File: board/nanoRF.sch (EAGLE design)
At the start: 21 parts

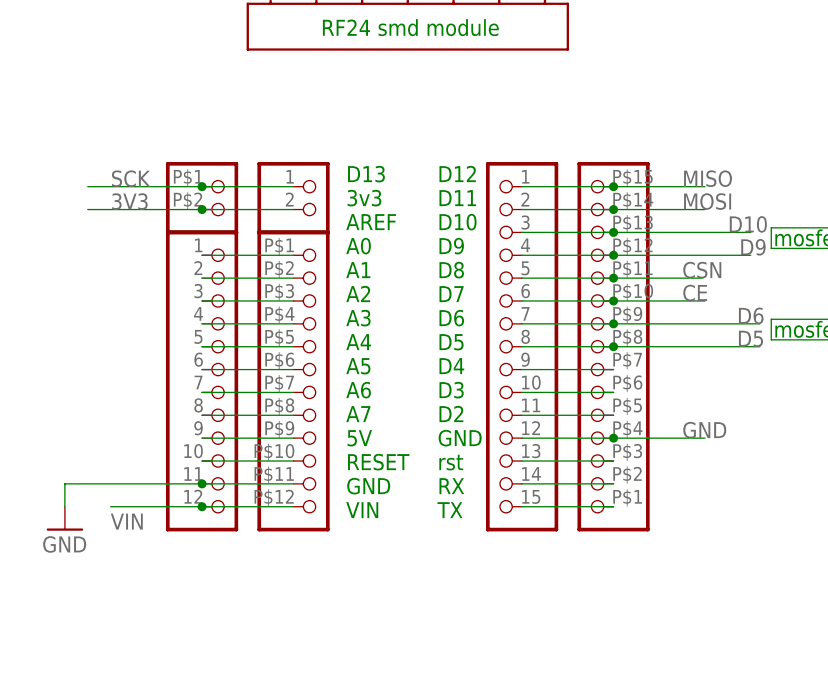
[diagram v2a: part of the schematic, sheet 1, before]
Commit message: removed reset and aref
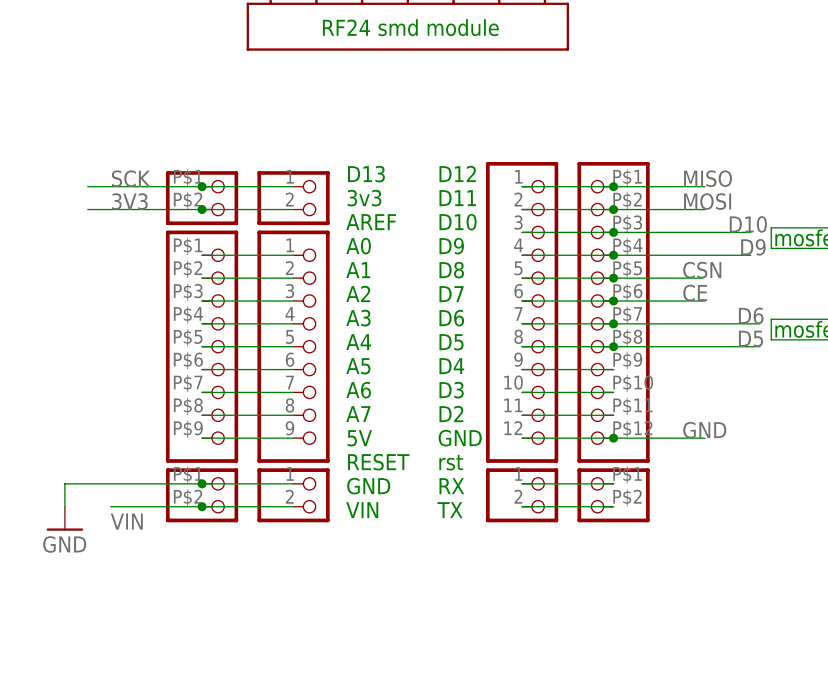
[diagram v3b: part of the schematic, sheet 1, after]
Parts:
- removed JP2: (no value), nano24rf:HEADER-1X15RND
- removed JP3: (no value), nano24rf:HEADER-1X15LONG
- added U$12, U$16: HEADER_1X2ROUND, nanoRF:HEADER_1X2ROUND
- added U$13, U$15: HEADER_1X2LONG, nanoRF:HEADER_1X2LONG
- added U$14: HEADER-1X12LONG, nanoRF:HEADER-1X12LONG
- added U$18: HEADER-1X12ROUND, nanoRF:HEADER-1X12ROUND
- U$6: value HEADER-1X12LONG -> HEADER-1X09RND; device nanoRF:HEADER-1X12LONG -> nanoRF:HEADER-1X09RND
- U$7: value HEADER-1X12ROUND -> HEADER-1X09LONG; device nanoRF:HEADER-1X12ROUND -> nanoRF:HEADER-1X09LONG
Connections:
- removed net N$10: U$6.10, U$7.10
- removed net N$13: JP2.13, JP3.3
- net CE: now also U$14.6, U$18.6; no longer JP2.6, JP3.10
- net CSN: now also U$14.5, U$18.5; no longer JP2.5, JP3.11
- net D10: now also U$14.3, U$18.3; no longer JP2.3, JP3.13
- net D5: now also U$14.8, U$18.8; no longer JP2.8, JP3.8
- net D6: now also U$14.7, U$18.7; no longer JP2.7, JP3.9
- net D9: now also U$14.4, U$18.4; no longer JP2.4, JP3.12
- net GND: now also U$12.1, U$13.1, U$14.12, U$18.12; no longer JP2.12, JP3.4, U$6.11, U$7.11
- net MISO: now also U$14.1, U$18.1; no longer JP2.1, JP3.15
- net MOSI: now also U$14.2, U$18.2; no longer JP2.2, JP3.14
- net N$11: now also U$15.2, U$16.2; no longer JP2.15, JP3.1
- net N$12: now also U$15.1, U$16.1; no longer JP2.14, JP3.2
- net N$14: now also U$14.11, U$18.11; no longer JP2.11, JP3.5
- net N$15: now also U$14.10, U$18.10; no longer JP2.10, JP3.6
- net N$16: now also U$14.9, U$18.9; no longer JP2.9, JP3.7
- net VIN: now also U$12.2, U$13.2; no longer U$6.12, U$7.12

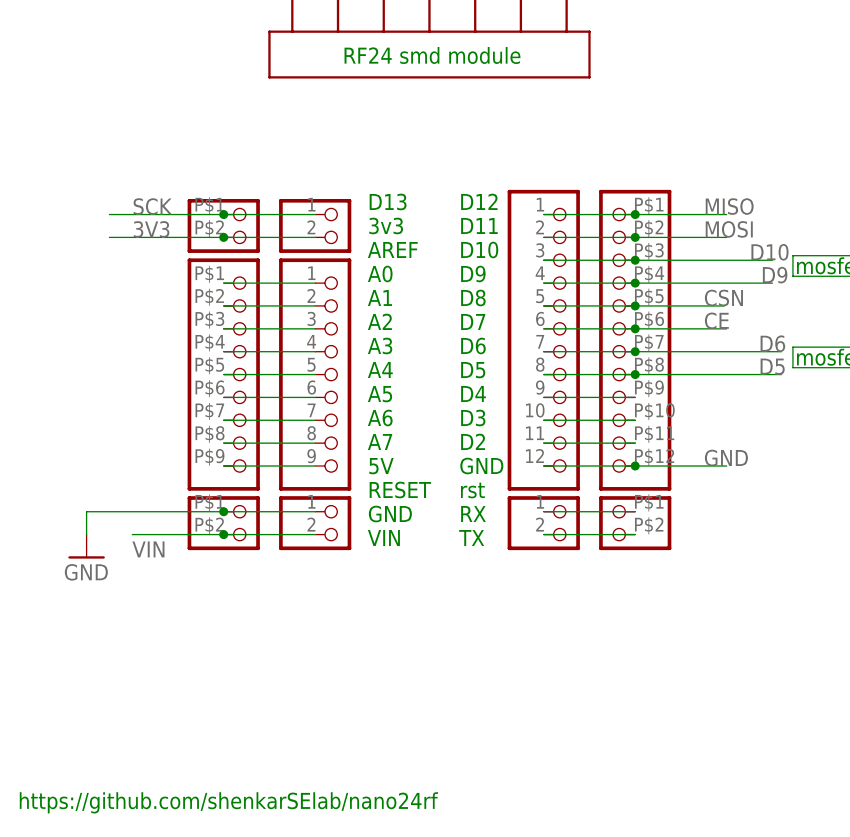
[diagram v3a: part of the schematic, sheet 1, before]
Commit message: revert to green ver, with gnd fix
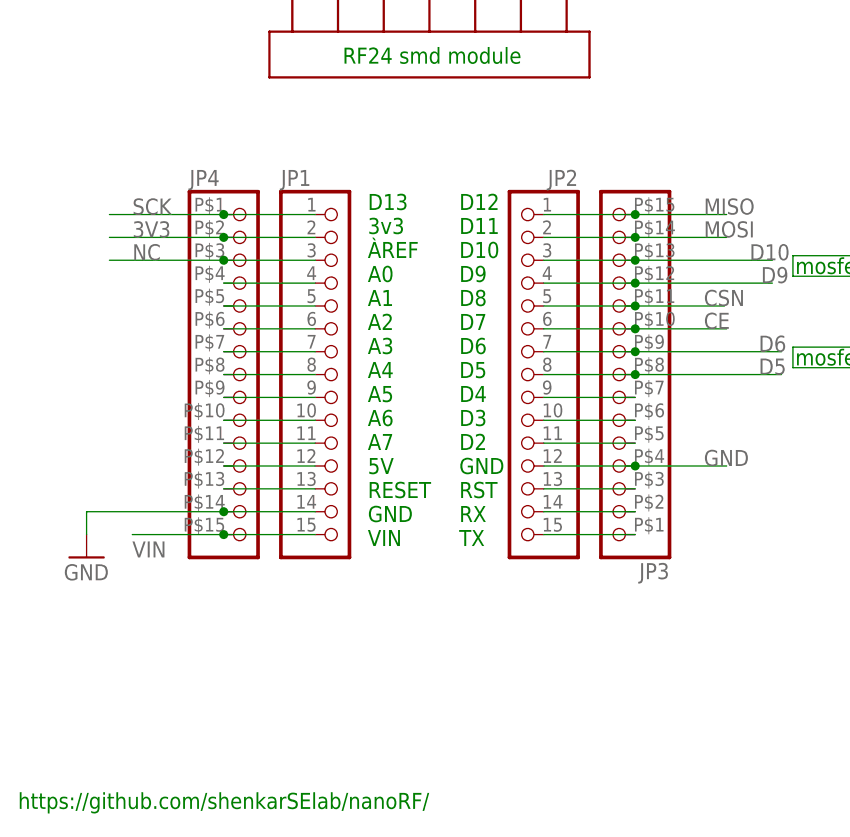
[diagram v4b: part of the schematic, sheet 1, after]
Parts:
- removed U$11, U$12, U$16: HEADER_1X2ROUND, nanoRF:HEADER_1X2ROUND
- removed U$13, U$15, U$8: HEADER_1X2LONG, nanoRF:HEADER_1X2LONG
- removed U$14: HEADER-1X12LONG, nanoRF:HEADER-1X12LONG
- removed U$18: HEADER-1X12ROUND, nanoRF:HEADER-1X12ROUND
- removed U$6: HEADER-1X09RND, nanoRF:HEADER-1X09RND
- removed U$7: HEADER-1X09LONG, nanoRF:HEADER-1X09LONG
- added JP1, JP2: (no value), nano24rf:HEADER-1X15RND
- added JP3, JP4: (no value), nano24rf:HEADER-1X15LONG
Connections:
- new net N$10: JP1.13, JP4.13
- new net N$13: JP2.13, JP3.3
- new net NC: JP1.3, JP4.3
- net 3V3: now also JP1.2, JP4.2; no longer U$11.2, U$8.2
- net CE: now also JP2.6, JP3.10; no longer U$14.6, U$18.6
- net CSN: now also JP2.5, JP3.11; no longer U$14.5, U$18.5
- net D10: now also JP2.3, JP3.13; no longer U$14.3, U$18.3
- net D5: now also JP2.8, JP3.8; no longer U$14.8, U$18.8
- net D6: now also JP2.7, JP3.9; no longer U$14.7, U$18.7
- net D9: now also JP2.4, JP3.12; no longer U$14.4, U$18.4
- net GND: now also JP1.14, JP2.12, JP3.4, JP4.14; no longer U$12.1, U$13.1, U$14.12, U$18.12
- net MISO: now also JP2.1, JP3.15; no longer U$14.1, U$18.1
- net MOSI: now also JP2.2, JP3.14; no longer U$14.2, U$18.2
- net N$1: now also JP1.4, JP4.4; no longer U$6.1, U$7.1
- net N$11: now also JP2.15, JP3.1; no longer U$15.2, U$16.2
- net N$12: now also JP2.14, JP3.2; no longer U$15.1, U$16.1
- net N$14: now also JP2.11, JP3.5; no longer U$14.11, U$18.11
- net N$15: now also JP2.10, JP3.6; no longer U$14.10, U$18.10
- net N$16: now also JP2.9, JP3.7; no longer U$14.9, U$18.9
- net N$2: now also JP1.5, JP4.5; no longer U$6.2, U$7.2
- net N$3: now also JP1.6, JP4.6; no longer U$6.3, U$7.3
- net N$4: now also JP1.7, JP4.7; no longer U$6.4, U$7.4
- net N$5: now also JP1.8, JP4.8; no longer U$6.5, U$7.5
- net N$6: now also JP1.9, JP4.9; no longer U$6.6, U$7.6
- net N$7: now also JP1.10, JP4.10; no longer U$6.7, U$7.7
- net N$8: now also JP1.11, JP4.11; no longer U$6.8, U$7.8
- net N$9: now also JP1.12, JP4.12; no longer U$6.9, U$7.9
- net SCK: now also JP1.1, JP4.1; no longer U$11.1, U$8.1
- net VIN: now also JP1.15, JP4.15; no longer U$12.2, U$13.2
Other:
- note added: "D12 D11 D10 D9 D8 D7 D6 D5 D4 D3 D2 GND RST RX TX"
- note added: "D13 3v3 ÀREF A0 A1 A2 A3 A4 A5 A6 A7 5V RESET GND VIN"
- note added: "NANO"
- note added: "https://github.com/shenkarSElab/nanoRF/"
- note removed: "D12 D11 D10 D9 D8 D7 D6 D5 D4 D3 D2 GND rst RX TX"
- note removed: "D13 3v3 AREF A0 A1 A2 A3 A4 A5 A6 A7 5V RESET GND VIN"
- note removed: "NANO pinout"
- note removed: "https://github.com/shenkarSElab/nano24rf"

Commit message: added schema
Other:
- moved on the sheet: D3, D4, Q3, Q4, R5, R6
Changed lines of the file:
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@@
 <part name="JP3" library="nano24rf" deviceset="HEADER-1X15" device="LONG"/>
 <part name="JP4" library="nano24rf" deviceset="HEADER-1X15" device="LONG"/>
+<part name="FRAME1" library="frames" library_urn="urn:adsk.eagle:library:229" deviceset="A4L-LOC" device=""/>
 </parts>
 <sheets>
@@
 <instance part="D2" gate="D" x="157.48" y="71.12" rot="R180"/>
 <instance part="U$1" gate="1" x="160.02" y="53.34"/>
-<instance part="Q3" gate="G$1" x="228.6" y="33.02"/>
-<instance part="D3" gate="D" x="228.6" y="40.64" smashed="yes" rot="R180">
-<attribute name="NAME" x="226.06" y="40.1574" size="1.778" layer="95" rot="R180"/>
-<attribute name="VALUE" x="226.06" y="42.9514" size="1.778" layer="96" rot="R180"/>
+<instance part="Q3" gate="G$1" x="162.56" y="96.52"/>
+<instance part="D3" gate="D" x="162.56" y="104.14" smashed="yes" rot="R180">
+<attribute name="NAME" x="160.02" y="103.6574" size="1.778" layer="95" rot="R180"/>
+<attribute name="VALUE" x="160.02" y="106.4514" size="1.778" layer="96" rot="R180"/>
 </instance>
-<instance part="U$2" gate="1" x="231.14" y="22.86"/>
-<instance part="Q4" gate="G$1" x="228.6" y="60.96"/>
-<instance part="D4" gate="D" x="228.6" y="68.58" rot="R180"/>
-<instance part="U$4" gate="1" x="231.14" y="50.8"/>
-<instance part="MOSFET-34" gate="G$1" x="269.24" y="43.18" rot="R90"/>
+<instance part="U$2" gate="1" x="165.1" y="86.36"/>
+<instance part="Q4" gate="G$1" x="162.56" y="124.46"/>
+<instance part="D4" gate="D" x="162.56" y="132.08" rot="R180"/>
+<instance part="U$4" gate="1" x="165.1" y="114.3"/>
+<instance part="MOSFET-34" gate="G$1" x="203.2" y="106.68" rot="R90"/>
 <instance part="MOSFET-12" gate="G$1" x="198.12" y="45.72" rot="R90"/>
 <instance part="R4" gate="G$1" x="152.4" y="55.88" rot="R90"/>
 <instance part="R3" gate="G$1" x="152.4" y="27.94" rot="R90"/>
-<instance part="R6" gate="G$1" x="223.52" y="53.34" rot="R90"/>
-<instance part="R5" gate="G$1" x="223.52" y="25.4" rot="R90"/>
-<instance part="U$9" gate="1" x="261.62" y="53.34" rot="R270"/>
+<instance part="R6" gate="G$1" x="157.48" y="116.84" rot="R90"/>
+<instance part="R5" gate="G$1" x="157.48" y="88.9" rot="R90"/>
+<instance part="U$9" gate="1" x="195.58" y="116.84" rot="R270"/>
 <instance part="U$10" gate="1" x="187.96" y="55.88" rot="R270"/>
 <instance part="JP3" gate="G$1" x="76.2" y="48.26" rot="R180"/>
 <instance part="JP4" gate="G$1" x="35.56" y="48.26"/>
+<instance part="FRAME1" gate="G$1" x="2.54" y="-17.78"/>
 </instances>
 <busses>
@@
 <pinref part="Q3" gate="G$1" pin="S"/>
 <pinref part="U$2" gate="1" pin="GND"/>
-<wire x1="231.14" y1="25.4" x2="231.14" y2="27.94" width="0.1524" layer="91"/>
+<wire x1="165.1" y1="88.9" x2="165.1" y2="91.44" width="0.1524" layer="91"/>
 <pinref part="R5" gate="G$1" pin="1"/>
-<wire x1="223.52" y1="20.32" x2="226.06" y2="20.32" width="0.1524" layer="91"/>
-<wire x1="226.06" y1="20.32" x2="226.06" y2="25.4" width="0.1524" layer="91"/>
-<wire x1="226.06" y1="25.4" x2="231.14" y2="25.4" width="0.1524" layer="91"/>
-<junction x="231.14" y="25.4"/>
+<wire x1="157.48" y1="83.82" x2="160.02" y2="83.82" width="0.1524" layer="91"/>
+<wire x1="160.02" y1="83.82" x2="160.02" y2="88.9" width="0.1524" layer="91"/>
+<wire x1="160.02" y1="88.9" x2="165.1" y2="88.9" width="0.1524" layer="91"/>
+<junction x="165.1" y="88.9"/>
 </segment>
 <segment>
 <pinref part="Q4" gate="G$1" pin="S"/>
 <pinref part="U$4" gate="1" pin="GND"/>
-<wire x1="231.14" y1="53.34" x2="231.14" y2="55.88" width="0.1524" layer="91"/>
+<wire x1="165.1" y1="116.84" x2="165.1" y2="119.38" width="0.1524" layer="91"/>
 <pinref part="R6" gate="G$1" pin="1"/>
-<wire x1="223.52" y1="48.26" x2="226.06" y2="48.26" width="0.1524" layer="91"/>
-<wire x1="226.06" y1="48.26" x2="226.06" y2="53.34" width="0.1524" layer="91"/>
-<wire x1="226.06" y1="53.34" x2="231.14" y2="53.34" width="0.1524" layer="91"/>
-<junction x="231.14" y="53.34"/>
+<wire x1="157.48" y1="111.76" x2="160.02" y2="111.76" width="0.1524" layer="91"/>
+<wire x1="160.02" y1="111.76" x2="160.02" y2="116.84" width="0.1524" layer="91"/>
+<wire x1="160.02" y1="116.84" x2="165.1" y2="116.84" width="0.1524" layer="91"/>
+<junction x="165.1" y="116.84"/>
 </segment>
 <segment>
@@
 <pinref part="U$9" gate="1" pin="GND"/>
 <pinref part="MOSFET-34" gate="G$1" pin="P$4"/>
-<wire x1="264.16" y1="53.34" x2="266.7" y2="53.34" width="0.1524" layer="91"/>
+<wire x1="198.12" y1="116.84" x2="200.66" y2="116.84" width="0.1524" layer="91"/>
 </segment>
 </net>
@@
 </segment>
 <segment>
-<wire x1="266.7" y1="43.18" x2="246.38" y2="43.18" width="0.1524" layer="91"/>
-<label x="243.84" y="43.18" size="1.778" layer="95"/>
+<wire x1="200.66" y1="106.68" x2="180.34" y2="106.68" width="0.1524" layer="91"/>
+<label x="177.8" y="106.68" size="1.778" layer="95"/>
 <pinref part="MOSFET-34" gate="G$1" pin="P$2"/>
 </segment>
 <segment>
 <pinref part="D4" gate="D" pin="C"/>
-<wire x1="218.44" y1="68.58" x2="226.06" y2="68.58" width="0.1524" layer="91"/>
-<label x="218.44" y="68.58" size="1.778" layer="95"/>
+<wire x1="152.4" y1="132.08" x2="160.02" y2="132.08" width="0.1524" layer="91"/>
+<label x="152.4" y="132.08" size="1.778" layer="95"/>
 </segment>
 <segment>
 <pinref part="D3" gate="D" pin="C"/>
-<wire x1="226.06" y1="40.64" x2="218.44" y2="40.64" width="0.1524" layer="91"/>
-<label x="218.44" y="40.64" size="1.778" layer="95"/>
+<wire x1="160.02" y1="104.14" x2="152.4" y2="104.14" width="0.1524" layer="91"/>
+<label x="152.4" y="104.14" size="1.778" layer="95"/>
 </segment>
 </net>
@@
 </segment>
 <segment>
-<label x="213.36" y="58.42" size="1.778" layer="95"/>
+<label x="147.32" y="121.92" size="1.778" layer="95"/>
 <pinref part="Q4" gate="G$1" pin="G"/>
-<wire x1="223.52" y1="58.42" x2="226.06" y2="58.42" width="0.1524" layer="91"/>
+<wire x1="157.48" y1="121.92" x2="160.02" y2="121.92" width="0.1524" layer="91"/>
 <pinref part="R6" gate="G$1" pin="2"/>
-<wire x1="223.52" y1="58.42" x2="215.9" y2="58.42" width="0.1524" layer="91"/>
-<junction x="223.52" y="58.42"/>
+<wire x1="157.48" y1="121.92" x2="149.86" y2="121.92" width="0.1524" layer="91"/>
+<junction x="157.48" y="121.92"/>
 </segment>
 </net>
@@
 <pinref part="Q3" gate="G$1" pin="D"/>
 <pinref part="D3" gate="D" pin="A"/>
-<wire x1="231.14" y1="38.1" x2="231.14" y2="40.64" width="0.1524" layer="91"/>
-<junction x="231.14" y="40.64"/>
-<wire x1="266.7" y1="38.1" x2="243.84" y2="38.1" width="0.1524" layer="91"/>
-<wire x1="243.84" y1="38.1" x2="243.84" y2="40.64" width="0.1524" layer="91"/>
-<wire x1="243.84" y1="40.64" x2="231.14" y2="40.64" width="0.1524" layer="91"/>
+<wire x1="165.1" y1="101.6" x2="165.1" y2="104.14" width="0.1524" layer="91"/>
+<junction x="165.1" y="104.14"/>
+<wire x1="200.66" y1="101.6" x2="177.8" y2="101.6" width="0.1524" layer="91"/>
+<wire x1="177.8" y1="101.6" x2="177.8" y2="104.14" width="0.1524" layer="91"/>
+<wire x1="177.8" y1="104.14" x2="165.1" y2="104.14" width="0.1524" layer="91"/>
 <pinref part="MOSFET-34" gate="G$1" pin="P$1"/>
-<label x="251.46" y="38.1" size="1.778" layer="95"/>
+<label x="185.42" y="101.6" size="1.778" layer="95"/>
 </segment>
 </net>
@@
 <pinref part="Q4" gate="G$1" pin="D"/>
 <pinref part="D4" gate="D" pin="A"/>
-<wire x1="231.14" y1="66.04" x2="231.14" y2="68.58" width="0.1524" layer="91"/>
-<junction x="231.14" y="68.58"/>
-<wire x1="246.38" y1="68.58" x2="231.14" y2="68.58" width="0.1524" layer="91"/>
-<wire x1="266.7" y1="48.26" x2="246.38" y2="48.26" width="0.1524" layer="91"/>
-<wire x1="246.38" y1="48.26" x2="246.38" y2="68.58" width="0.1524" layer="91"/>
+<wire x1="165.1" y1="129.54" x2="165.1" y2="132.08" width="0.1524" layer="91"/>
+<junction x="165.1" y="132.08"/>
+<wire x1="180.34" y1="132.08" x2="165.1" y2="132.08" width="0.1524" layer="91"/>
+<wire x1="200.66" y1="111.76" x2="180.34" y2="111.76" width="0.1524" layer="91"/>
+<wire x1="180.34" y1="111.76" x2="180.34" y2="132.08" width="0.1524" layer="91"/>
 <pinref part="MOSFET-34" gate="G$1" pin="P$3"/>
-<label x="251.46" y="48.26" size="1.778" layer="95"/>
+<label x="185.42" y="111.76" size="1.778" layer="95"/>
 </segment>
 </net>
@@
 </segment>
 <segment>
-<label x="213.36" y="30.48" size="1.778" layer="95"/>
+<label x="147.32" y="93.98" size="1.778" layer="95"/>
 <pinref part="Q3" gate="G$1" pin="G"/>
-<wire x1="223.52" y1="30.48" x2="226.06" y2="30.48" width="0.1524" layer="91"/>
+<wire x1="157.48" y1="93.98" x2="160.02" y2="93.98" width="0.1524" layer="91"/>
 <pinref part="R5" gate="G$1" pin="2"/>
-<wire x1="215.9" y1="30.48" x2="223.52" y2="30.48" width="0.1524" layer="91"/>
-<junction x="223.52" y="30.48"/>
+<wire x1="149.86" y1="93.98" x2="157.48" y2="93.98" width="0.1524" layer="91"/>
+<junction x="157.48" y="93.98"/>
 </segment>
 </net>
@@
 which will not be processed correctly with this version.
 </note>
+<note version="8.2" severity="warning">
+Since Version 8.2, EAGLE supports online libraries. The ids
+of those online libraries will not be understood (or retained)
+with this version.
+</note>
+<note version="8.3" severity="warning">
+Since Version 8.3, EAGLE supports URNs for individual library
+assets (packages, symbols, and devices). The URNs of those assets
+will not be understood (or retained) with this version.
+</note>
 </compatibility>
